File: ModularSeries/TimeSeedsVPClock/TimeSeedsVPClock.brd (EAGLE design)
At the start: 85 x 50 mm, 75 parts, among them T1 2N3904

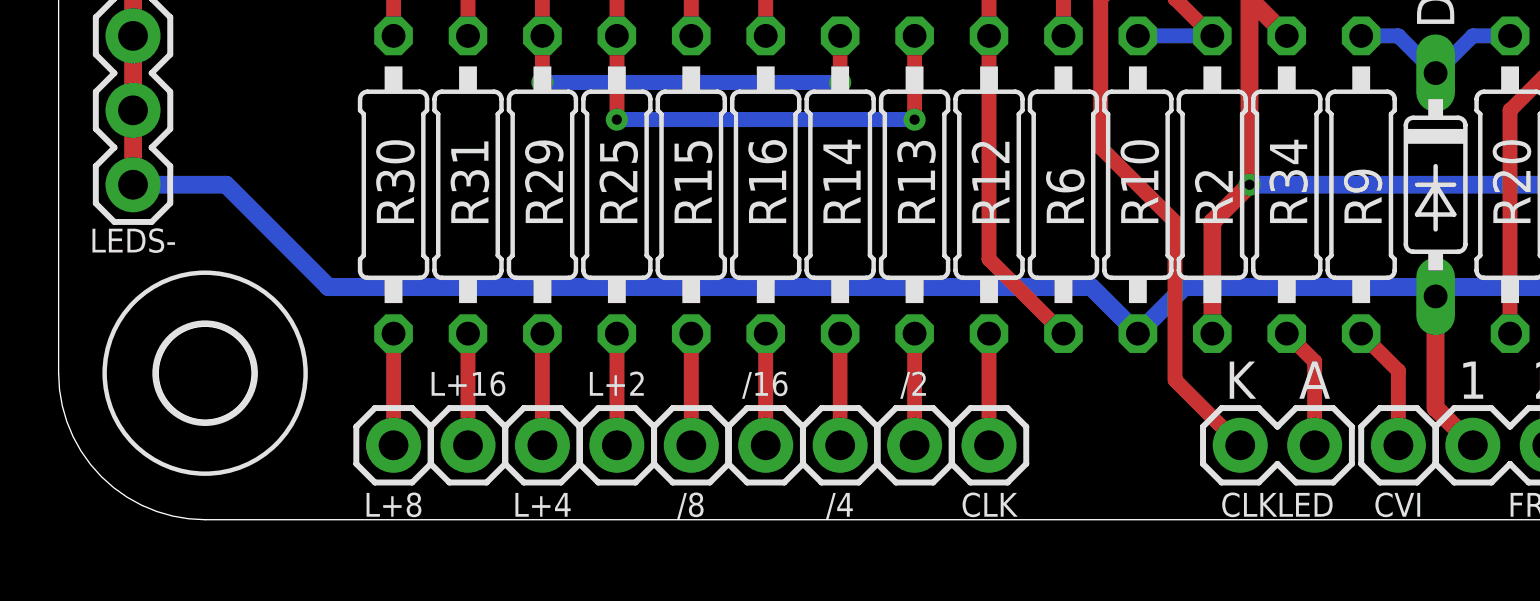
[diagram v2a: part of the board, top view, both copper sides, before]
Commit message: Updates to ARFG schematic - not included in layout yet
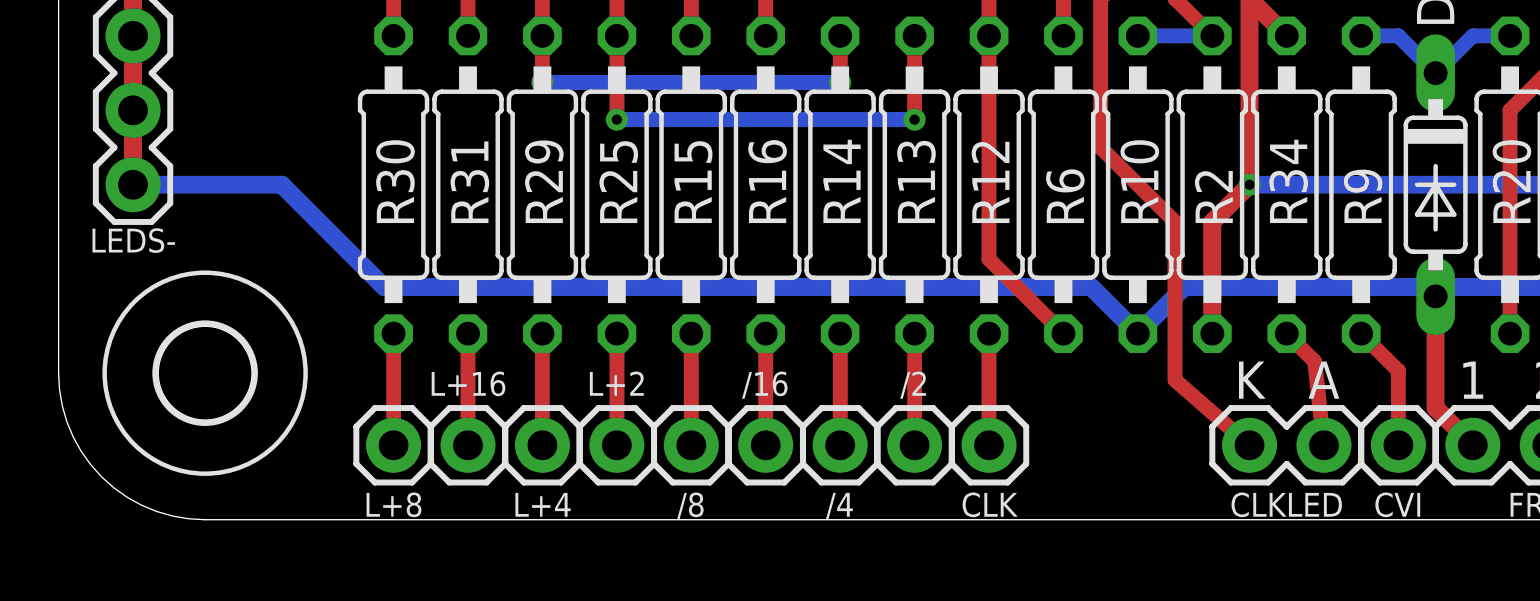
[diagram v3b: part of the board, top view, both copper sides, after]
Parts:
- moved CLKLED 0.32 mm to (40.6, 2.54)
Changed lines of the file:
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@@
 Taylor
 2020</text>
-<text x="42.8625" y="4.7625" size="1.27" layer="21" font="vector" ratio="16" align="center">A</text>
-<text x="40.3225" y="4.7625" size="1.27" layer="21" font="vector" ratio="16" align="center">K</text>
+<text x="43.18" y="4.7625" size="1.27" layer="21" font="vector" ratio="16" align="center">A</text>
+<text x="40.64" y="4.7625" size="1.27" layer="21" font="vector" ratio="16" align="center">K</text>
 <text x="48.26" y="4.7625" size="1.27" layer="21" font="vector" ratio="16" align="center">1</text>
 <text x="50.8" y="4.7625" size="1.27" layer="21" font="vector" ratio="16" align="center">2</text>
@@
 <attribute name="VALUE" x="38.1" y="36.195" size="1.27" layer="27" ratio="10" rot="R270"/>
 </element>
-<element name="CLKLED" library="ElectricNoodleBox" package="1X02" value="2XWIREPAD" x="40.3225" y="2.54" smashed="yes">
-<attribute name="NAME" x="41.5925" y="0.508" size="0.8128" layer="25" font="vector" ratio="20" rot="R180" align="center"/>
-<attribute name="VALUE" x="40.3225" y="4.318" size="0.6096" layer="27" font="vector" ratio="20"/>
+<element name="CLKLED" library="ElectricNoodleBox" package="1X02" value="2XWIREPAD" x="40.64" y="2.54" smashed="yes">
+<attribute name="NAME" x="41.91" y="0.508" size="0.8128" layer="25" font="vector" ratio="20" rot="R180" align="center"/>
+<attribute name="VALUE" x="40.64" y="4.318" size="0.6096" layer="27" font="vector" ratio="20"/>
 </element>
 <element name="R32" library="rcl" library_urn="urn:adsk.eagle:library:334" package="0207/10" package3d_urn="urn:adsk.eagle:package:23491/2" value="100Ω" x="43.18" y="39.37" smashed="yes" rot="R90">
@@
 <wire x1="46.99" y1="3.81" x2="46.99" y2="7.62" width="0.6096" layer="1"/>
 <wire x1="36.83" y1="6.35" x2="35.2425" y2="7.9375" width="0.6096" layer="16"/>
-<wire x1="9.2075" y1="7.9375" x2="5.715" y2="11.43" width="0.6096" layer="16"/>
-<wire x1="5.715" y1="11.43" x2="2.54" y2="11.43" width="0.6096" layer="16"/>
-<wire x1="35.2425" y1="7.9375" x2="9.2075" y2="7.9375" width="0.6096" layer="16"/>
+<wire x1="11.1125" y1="7.9375" x2="7.62" y2="11.43" width="0.6096" layer="16"/>
+<wire x1="7.62" y1="11.43" x2="2.54" y2="11.43" width="0.6096" layer="16"/>
+<wire x1="35.2425" y1="7.9375" x2="11.1125" y2="7.9375" width="0.6096" layer="16"/>
 <wire x1="36.83" y1="6.35" x2="38.4175" y2="7.9375" width="0.6096" layer="16"/>
 <wire x1="46.6725" y1="7.9375" x2="46.99" y2="7.62" width="0.6096" layer="16"/>
@@
 <contactref element="CLKLED" pad="2"/>
 <contactref element="R34" pad="1"/>
-<wire x1="42.8625" y1="2.54" x2="42.8625" y2="5.3975" width="0.508" layer="1"/>
+<wire x1="43.18" y1="2.54" x2="42.8625" y2="5.3975" width="0.508" layer="1"/>
 <wire x1="42.8625" y1="5.3975" x2="41.91" y2="6.35" width="0.508" layer="1"/>
 </signal>
@@
 <contactref element="CLKLED" pad="1"/>
 <contactref element="T1" pad="1"/>
-<wire x1="40.3225" y1="2.54" x2="38.1" y2="4.7625" width="0.508" layer="1"/>
+<wire x1="40.64" y1="2.54" x2="38.1" y2="4.7625" width="0.508" layer="1"/>
 <wire x1="35.56" y1="17.78" x2="36.83" y2="19.05" width="0.508" layer="1"/>
 <wire x1="36.83" y1="19.05" x2="36.83" y2="35.56" width="0.508" layer="1"/>

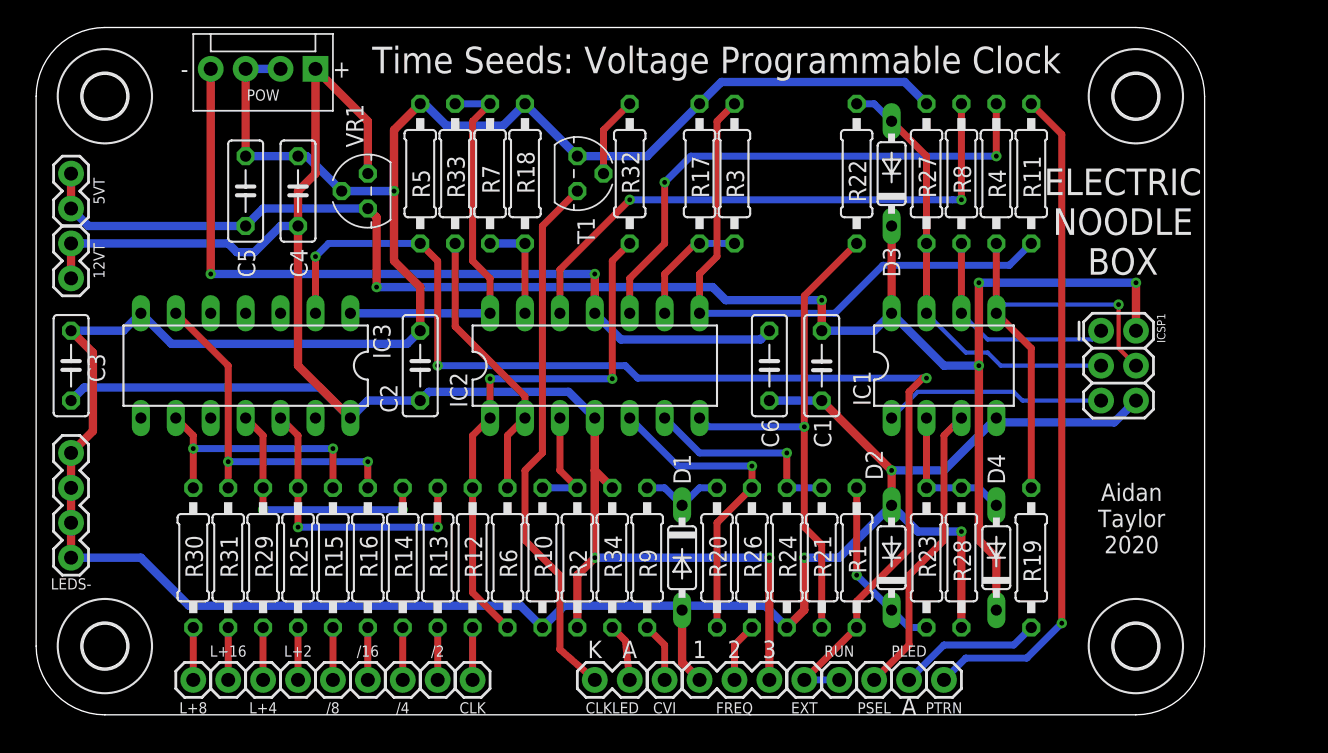
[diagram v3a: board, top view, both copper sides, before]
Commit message: Power header updated on most PCBs. Knives layout added
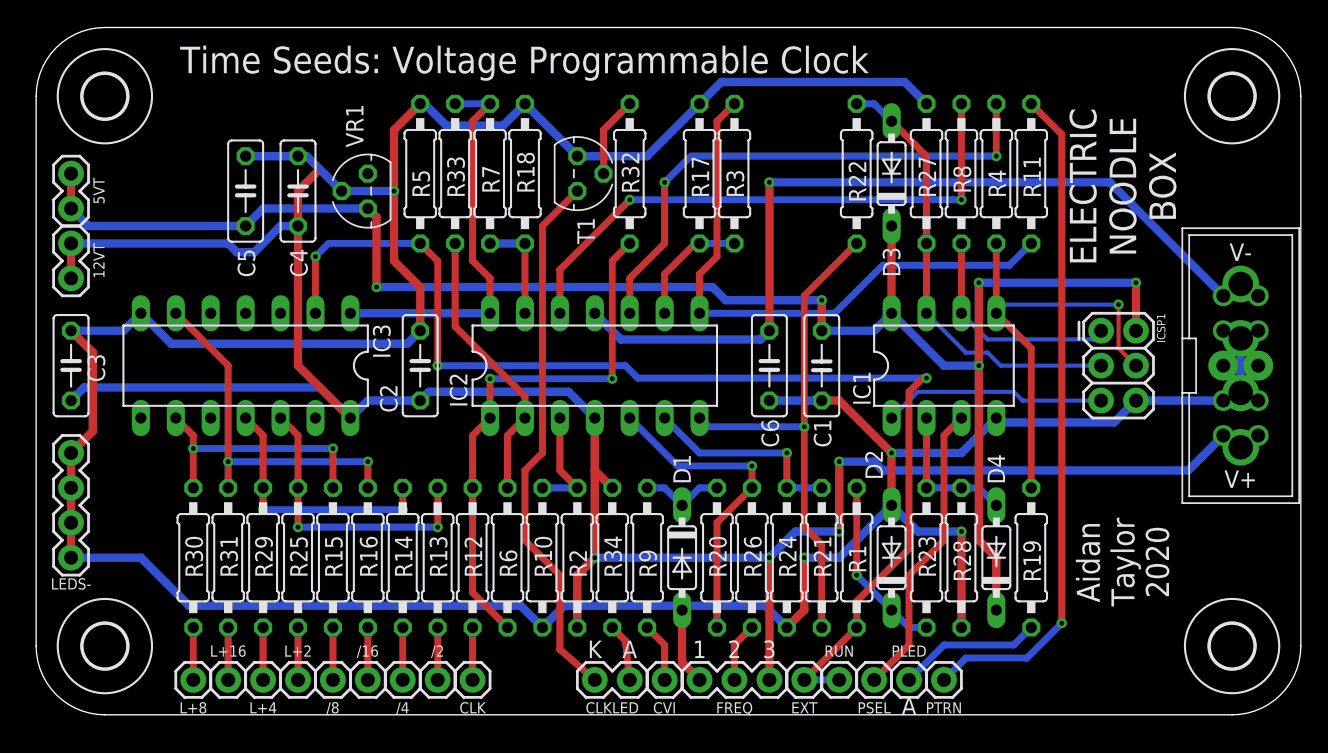
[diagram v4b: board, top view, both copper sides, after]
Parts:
- removed POW: 4XMOLEX, ElectricNoodleBox:MOLEX-1X4
- added WP1: COMBO_SUPPLY_HEADER, ElectricNoodleBox:COMBINED_POWER
- moved H2 7.00 mm to (87.0, 5.00)
- moved H3 7.00 mm to (87.0, 45.0)
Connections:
- net +12V: now also WP1.V+1, WP1.V+2, WP1.V+3; no longer POW.1
- net -12V: now also WP1.V-1, WP1.V-2, WP1.V-3; no longer POW.4
- net AGND: now also WP1.GND1, WP1.GND2, WP1.GND3, WP1.GND4, WP1.GND5, WP1.GND6, WP1.GND7, WP1.GND8; no longer POW.2, POW.3
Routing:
- net +12V: track 136.9 -> 163.6 mm, vias 2 -> 4
- net AGND: track 247.9 -> 258.1 mm
- net -12V: track 59.5 -> 64.2 mm, vias 2 -> 1
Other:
- board size 85 x 50 mm -> 92 x 50 mm
- board text removed: "+"
- board text removed: "-"

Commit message: Control PCBs for Prism, Portals, TimeSeeds and Knives added
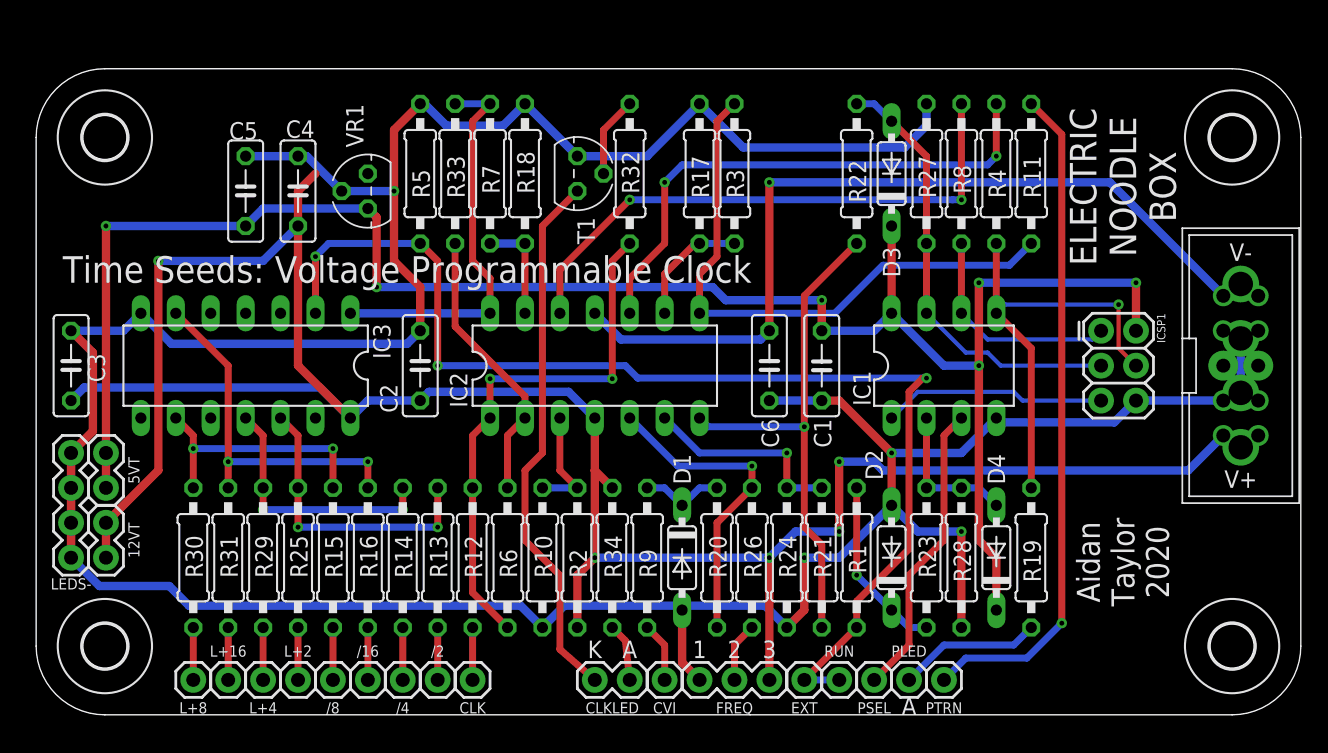
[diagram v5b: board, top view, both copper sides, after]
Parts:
- moved 12VT 20.5 mm to (5.08, 11.4)
- moved 5VT 20.5 mm to (5.08, 16.5)
- moved H3 3.00 mm to (87.0, 42.0)
- moved H4 3.00 mm to (5.00, 42.0)
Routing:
- net +12V: track 163.6 -> 177.9 mm, vias 4 -> 5
- net +5V: track 125.3 -> 138.8 mm, vias 5 -> 6
- net AGND: track 258.1 -> 260.4 mm
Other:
- board size 92 x 50 mm -> 92 x 47 mm

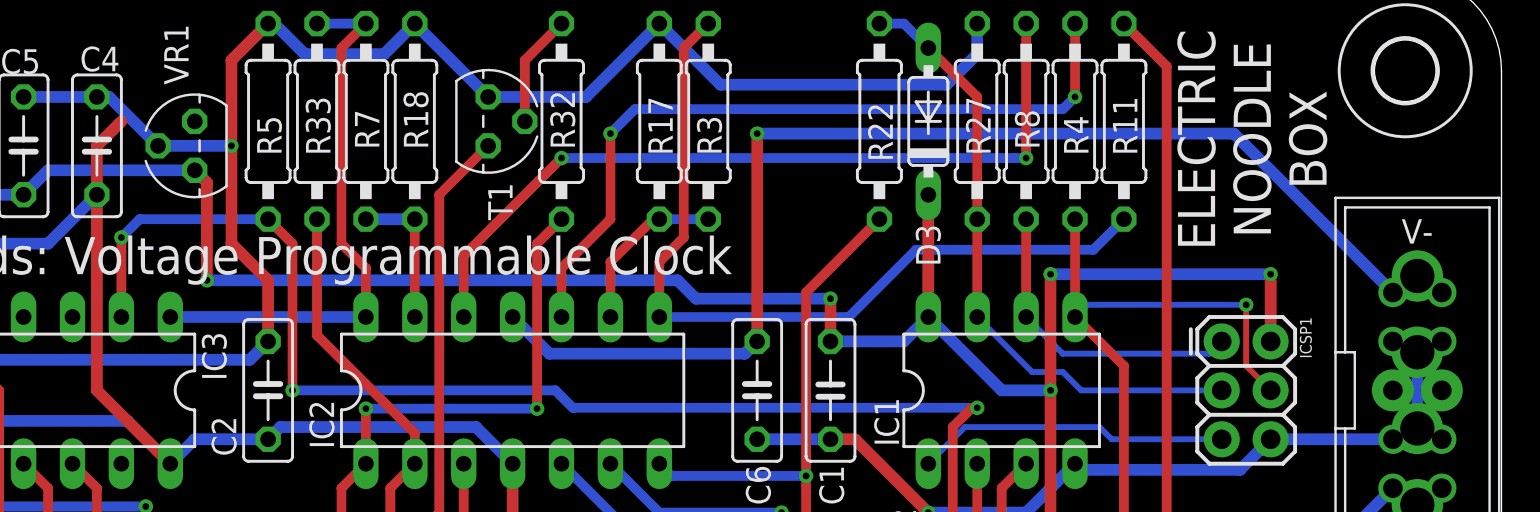
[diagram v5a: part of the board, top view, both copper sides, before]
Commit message: DRC check fixes on Prism, Portals, TimeSeeds and Knives
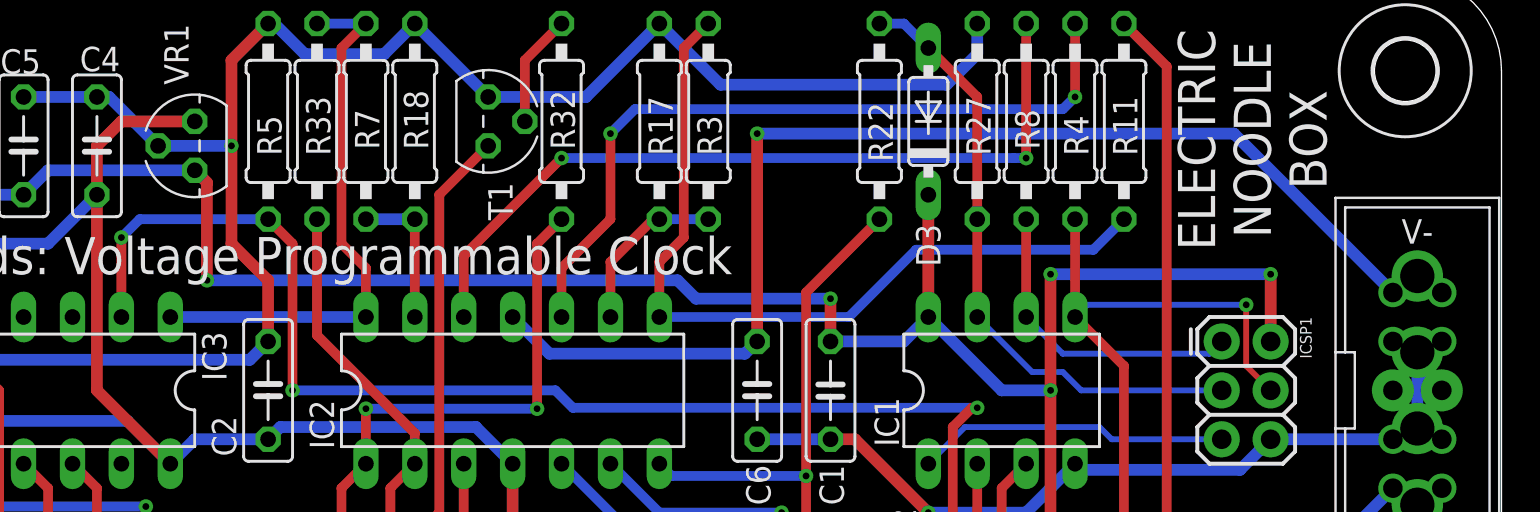
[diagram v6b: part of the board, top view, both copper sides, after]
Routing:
- net +12V: track 177.9 -> 181.7 mm
- net AGND: track 260.4 -> 262.9 mm
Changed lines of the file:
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@@
 <setting verticaltext="up"/>
 </settings>
-<grid distance="1" unitdist="mm" unit="mm" style="lines" multiple="1" display="no" altdistance="5" altunitdist="mil" altunit="mil"/>
+<grid distance="25" unitdist="mil" unit="mil" style="lines" multiple="1" display="no" altdistance="5" altunitdist="mil" altunit="mil"/>
 <layers>
 <layer number="1" name="Top" color="4" fill="1" visible="yes" active="yes"/>
@@
 <wire x1="2.54" y1="11.43" x2="4.6012" y2="9.3688" width="0.6096" layer="16"/>
 <wire x1="4.6012" y1="9.3688" x2="9.6812" y2="9.3688" width="0.6096" layer="16"/>
-<wire x1="87.63" y1="27.38" x2="88.9" y2="25.4" width="0" layer="19" extent="1-1"/>
+<wire x1="88.9" y1="25.4" x2="87.63" y2="26.67" width="0.6096" layer="16"/>
+<wire x1="87.63" y1="26.67" x2="87.63" y2="27.38" width="0.6096" layer="16"/>
 </signal>
 <signal name="MOSI">
@@
 <wire x1="8.89" y1="33.02" x2="8.89" y2="17.78" width="0.6096" layer="1"/>
 <wire x1="8.89" y1="17.78" x2="5.08" y2="13.97" width="0.6096" layer="1"/>
-<wire x1="20.32" y1="39.37" x2="24.13" y2="39.37" width="0" layer="19" extent="1-1"/>
+<wire x1="20.32" y1="39.37" x2="24.13" y2="39.37" width="0.6096" layer="1"/>
 </signal>
 <signal name="SCK">
@@
 <mfgpreviewcolor name="substratecolor" color="0xFF786E46"/>
 </mfgpreviewcolors>
+<errors>
+</errors>
 </board>
 </drawing>
